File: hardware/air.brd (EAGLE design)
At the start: 73.6 x 71.7 mm, 9 parts, among them J1 Air Digitals, J2 Air Analogs, U1 TGS2600, U2 DHT22

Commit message: Updates
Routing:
- net N$3: track 0.00 -> 46.8 mm
- net 3.3V: track 0.00 -> 43.3 mm
- net N$8: track 0.00 -> 32.4 mm
- net N$6: track 0.00 -> 31.1 mm
- net N$4: track 0.00 -> 29.9 mm
- net SDA: track 0.00 -> 15.1 mm
- net N$2: track 0.00 -> 14.6 mm
- net N$1: track 0.00 -> 13.2 mm
- added copper zone on layer 1, net GND
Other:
- board text added: "Polycase WC31F"

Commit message: eagle updates
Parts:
- removed R3: 10K, SparkFun-Passives:AXIAL-0.4
- removed R4: PHOTOCELLPTH, SparkFun-Sensors:PHOTOCELL
- added JP2: TSL2591 Breakout, microbuilder:1X06_ROUND_70
- moved U1 8.28 mm to (27.5, 52.6)
- moved R2 7.64 mm to (28.1, 43.5)
- moved R1 4.62 mm to (59.0, 36.9)
- moved J2 3.23 mm to (17.3, 54.4)
- moved J1 3.12 mm to (17.4, 31.0)
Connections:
- removed net N$6: J2.3, R3.P$1, R4.1
- net GND: now also JP2.2; no longer R4.2
- net N$1: now also JP2.1
- net N$2: now also JP2.6
- net N$8: no longer R3.P$2
- net SDA: now also JP2.5
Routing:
- net N$1: track 13.2 -> 48.2 mm
- net SDA: track 15.1 -> 47.3 mm
- net N$6: track 31.1 -> 0.00 mm
- net N$2: track 14.6 -> 43.4 mm
- net N$8: track 32.4 -> 12.1 mm
- net N$4: track 29.9 -> 22.0 mm
- net N$3: track 46.8 -> 51.8 mm
- net 3.3V: track 43.3 -> 44.3 mm

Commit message: remove light sensor from air board
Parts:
- removed JP2: TSL2591 Breakout, microbuilder:1X06_ROUND_70
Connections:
- net GND: no longer JP2.2
- net N$1: no longer JP2.1
- net N$2: no longer JP2.6
- net SDA: no longer JP2.5
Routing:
- net N$1: track 48.2 -> 16.3 mm
- net SDA: track 47.3 -> 18.0 mm
- net N$2: track 43.4 -> 17.5 mm
- net 3.3V: track 44.3 -> 47.8 mm
- net N$3: track 51.8 -> 52.7 mm
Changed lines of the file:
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@@
 <attribute name="VALUE" x="25.2476" y="58.2422" size="0.8128" layer="21" font="vector"/>
-</element>
-<element name="JP2" library="microbuilder" package="1X06_ROUND_70" value="TSL2591 Breakout" x="39.0144" y="53.2892" smashed="yes" rot="R270">
-<attribute name="NAME" x="38.4048" y="42.3418" size="0.8128" layer="25" ratio="18"/>
-<attribute name="VALUE" x="38.4556" y="40.9194" size="0.6096" layer="21" font="vector" ratio="12"/>
 </element>
 </elements>
@@
 <contactref element="J1" pad="1"/>
 <contactref element="JP1" pad="1"/>
-<contactref element="JP2" pad="1"/>
-<wire x1="17.4498" y1="30.988" x2="31.242" y2="30.988" width="1.016" layer="16"/>
-<wire x1="31.242" y1="30.988" x2="33.782" y2="30.988" width="1.016" layer="16"/>
-<wire x1="31.242" y1="51.816" x2="38.862" y2="59.436" width="1.016" layer="16"/>
-<wire x1="31.242" y1="30.988" x2="31.242" y2="51.816" width="1.016" layer="16"/>
-<wire x1="38.862" y1="59.436" x2="39.0144" y2="59.6392" width="1.016" layer="16"/>
+<wire x1="17.4498" y1="30.988" x2="33.782" y2="30.988" width="1.016" layer="16"/>
 </signal>
 <signal name="N$3">
@@
 <wire x1="59.182" y1="31.75" x2="59.182" y2="26.162" width="0.3048" layer="1"/>
 <wire x1="59.182" y1="31.75" x2="58.9534" y2="31.8516" width="0.3048" layer="1"/>
-<wire x1="19.558" y1="29.718" x2="17.526" y2="27.686" width="0.3048" layer="16"/>
-<wire x1="55.88" y1="29.718" x2="19.558" y2="29.718" width="0.3048" layer="16"/>
-<wire x1="57.912" y1="31.75" x2="55.88" y2="29.718" width="0.3048" layer="16"/>
-<wire x1="58.928" y1="31.75" x2="57.912" y2="31.75" width="0.3048" layer="16"/>
-<wire x1="17.526" y1="27.686" x2="17.4498" y2="27.488" width="0.3048" layer="16"/>
-<wire x1="58.928" y1="31.75" x2="58.9534" y2="31.8516" width="0.3048" layer="16"/>
+<wire x1="22.606" y1="32.766" x2="17.526" y2="27.686" width="0.3048" layer="1"/>
+<wire x1="58.42" y1="32.766" x2="22.606" y2="32.766" width="0.3048" layer="1"/>
+<wire x1="58.928" y1="32.258" x2="58.42" y2="32.766" width="0.3048" layer="1"/>
+<wire x1="58.928" y1="32.004" x2="58.928" y2="32.258" width="0.3048" layer="1"/>
+<wire x1="17.526" y1="27.686" x2="17.4498" y2="27.488" width="0.3048" layer="1"/>
+<wire x1="58.928" y1="32.004" x2="58.9534" y2="31.8516" width="0.3048" layer="1"/>
 </signal>
 <signal name="GND" class="1">
@@
 <vertex x="74.93" y="0"/>
 </polygon>
-<contactref element="JP2" pad="2"/>
 </signal>
 <signal name="3.3V">
@@
 <contactref element="U2" pad="VDD"/>
 <contactref element="R1" pad="P$2"/>
-<wire x1="60.96" y1="41.91" x2="60.96" y2="28.702" width="0.3048" layer="16"/>
-<wire x1="60.96" y1="28.702" x2="60.96" y2="26.924" width="0.3048" layer="16"/>
+<wire x1="60.96" y1="41.91" x2="60.96" y2="26.924" width="0.3048" layer="16"/>
 <wire x1="59.182" y1="41.91" x2="60.96" y2="41.91" width="0.3048" layer="16"/>
 <wire x1="59.182" y1="41.91" x2="58.9534" y2="42.0116" width="0.3048" layer="16"/>
-<wire x1="34.036" y1="28.702" x2="33.782" y2="28.448" width="0.3048" layer="16"/>
-<wire x1="60.96" y1="28.702" x2="34.036" y2="28.702" width="0.3048" layer="16"/>
+<wire x1="47.244" y1="41.91" x2="33.782" y2="28.448" width="0.3048" layer="16"/>
+<wire x1="58.928" y1="41.91" x2="47.244" y2="41.91" width="0.3048" layer="16"/>
+<wire x1="58.928" y1="41.91" x2="58.9534" y2="42.0116" width="0.3048" layer="16"/>
 </signal>
 <signal name="N$2">
 <contactref element="J1" pad="4"/>
 <contactref element="JP1" pad="4"/>
-<contactref element="JP2" pad="6"/>
 <wire x1="30.988" y1="20.574" x2="33.782" y2="23.368" width="0.3048" layer="16"/>
 <wire x1="17.526" y1="20.574" x2="30.988" y2="20.574" width="0.3048" layer="16"/>
 <wire x1="17.526" y1="20.574" x2="17.4498" y2="20.488" width="0.3048" layer="16"/>
-<wire x1="35.814" y1="43.688" x2="38.862" y2="46.736" width="0.3048" layer="1"/>
-<wire x1="35.814" y1="25.146" x2="35.814" y2="43.688" width="0.3048" layer="1"/>
-<wire x1="34.036" y1="23.368" x2="35.814" y2="25.146" width="0.3048" layer="1"/>
-<wire x1="33.782" y1="23.368" x2="34.036" y2="23.368" width="0.3048" layer="1"/>
-<wire x1="38.862" y1="46.736" x2="39.0144" y2="46.9392" width="0.3048" layer="1"/>
 </signal>
 <signal name="SDA">
 <contactref element="J1" pad="3"/>
 <contactref element="JP1" pad="5"/>
-<contactref element="JP2" pad="5"/>
 <wire x1="31.242" y1="23.368" x2="33.782" y2="20.828" width="0.3048" layer="1"/>
 <wire x1="17.526" y1="23.368" x2="31.242" y2="23.368" width="0.3048" layer="1"/>
 <wire x1="17.526" y1="23.876" x2="17.526" y2="23.368" width="0.3048" layer="1"/>
 <wire x1="17.526" y1="23.876" x2="17.4498" y2="23.988" width="0.3048" layer="1"/>
-<wire x1="35.052" y1="45.466" x2="38.862" y2="49.276" width="0.3048" layer="1"/>
-<wire x1="35.052" y1="35.306" x2="35.052" y2="45.466" width="0.3048" layer="1"/>
-<wire x1="31.242" y1="31.496" x2="35.052" y2="35.306" width="0.3048" layer="1"/>
-<wire x1="31.242" y1="23.368" x2="31.242" y2="31.496" width="0.3048" layer="1"/>
-<wire x1="38.862" y1="49.276" x2="39.0144" y2="49.4792" width="0.3048" layer="1"/>
 </signal>
 <signal name="N$8" class="1">

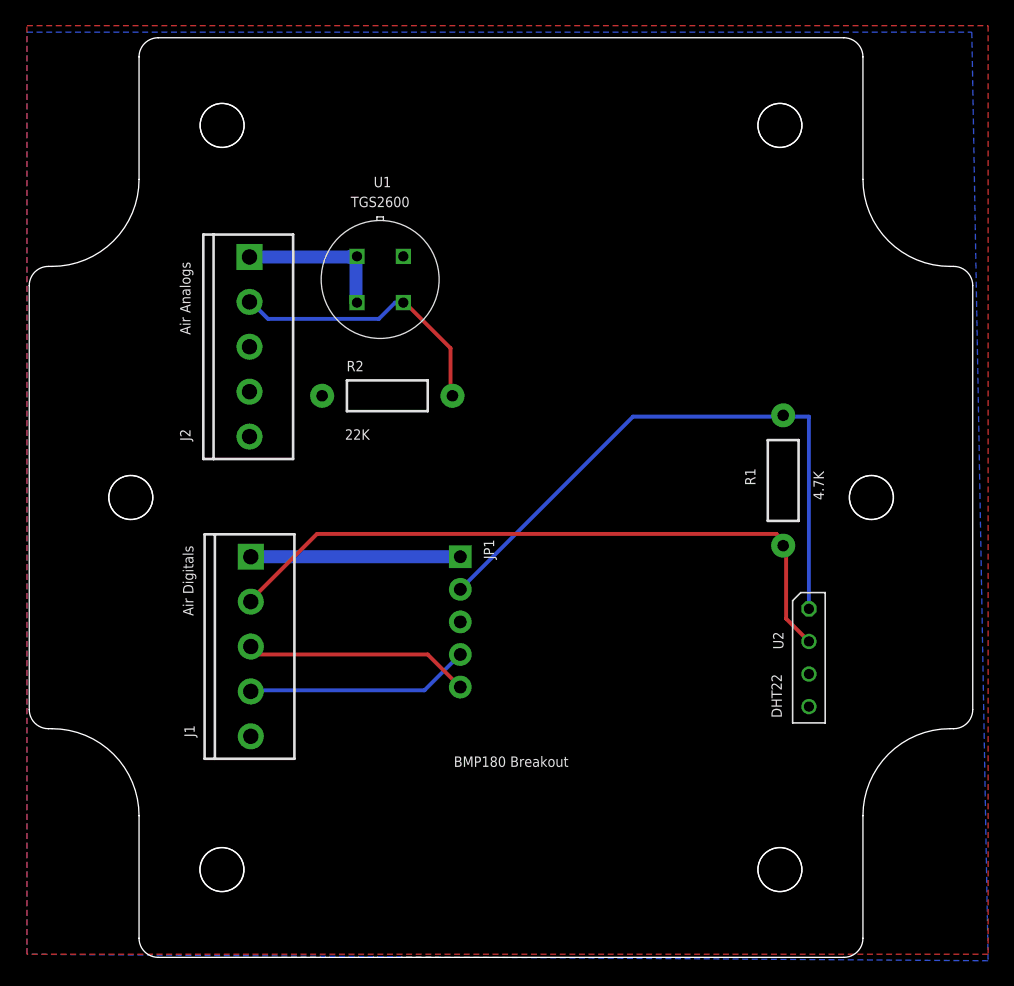
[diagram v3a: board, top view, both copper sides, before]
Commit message: Revise for Ambient Weather SRS100
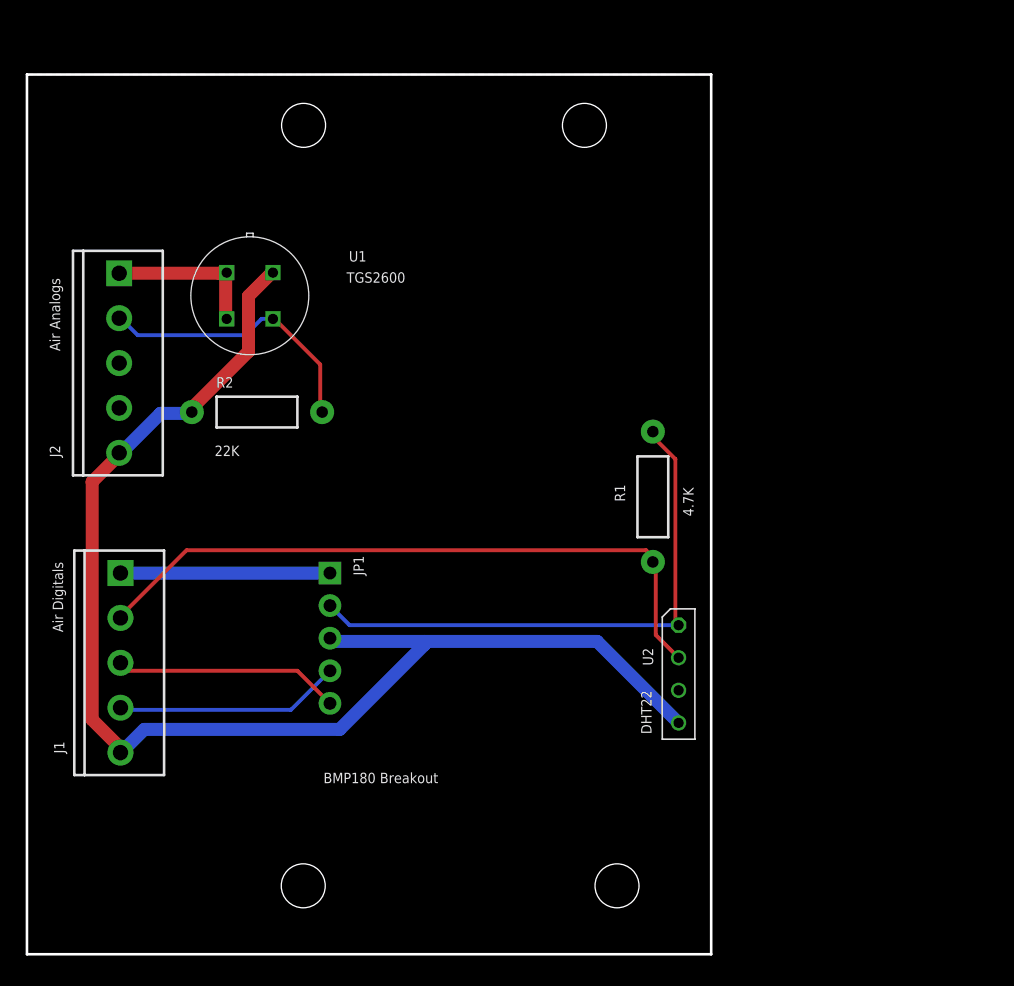
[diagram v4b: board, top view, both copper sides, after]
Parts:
- moved R1 10.2 mm to (48.8, 35.7)
- moved U2 10.2 mm to (50.8, 21.8)
- moved J1 10.2 mm to (7.29, 29.7)
- moved R2 10.2 mm to (17.9, 42.3)
- moved U1 10.2 mm to (17.4, 51.3)
- moved J2 10.2 mm to (7.19, 53.1)
- moved JP1 10.2 mm to (23.6, 24.6)
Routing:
- net GND: track 0.00 -> 103.0 mm
- net 3.3V: track 47.8 -> 43.8 mm
- added copper zone on layer 1, net N$5
- added copper zone on layer 16, net N$6
- removed copper zone on layer 1, net GND
- removed copper zone on layer 16, net GND
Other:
- board size 73.6 x 71.7 mm -> 53.3 x 68.6 mm
- board text removed: "Polycase WC31F"

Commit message: decoupling caps
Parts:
- added C1, C2, C3: 0.1uF, SparkFun-Capacitors:CAP-PTH-SMALL
- R2: value 22K -> 10K
- moved R1 6.48 mm to (47.5, 42.0)
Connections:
- net 3.3V: now also C2.1
- net GND: now also C1.2, C2.2, C3.2
- net N$1: now also C3.1
- net N$8: now also C1.1
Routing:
- net N$3: track 52.7 -> 65.6 mm
- net 3.3V: track 43.8 -> 51.0 mm
- net N$2: track 17.7 -> 23.4 mm
- net N$8: track 12.1 -> 17.6 mm
- net GND: track 103.0 -> 104.8 mm
